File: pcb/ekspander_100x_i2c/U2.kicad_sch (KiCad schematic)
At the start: 13 parts, among them J5 DG127A-5.08-06P-14-00AH, J6 DG127A-5.08-06P-14-00AH, J7 DG127A-5.08-06P-14-00AH, U14 LTV-847, U15 ITS716G, U16 ITS716G, U17 LTV-847, U18 LTV-847, U2 MCP23017_SP

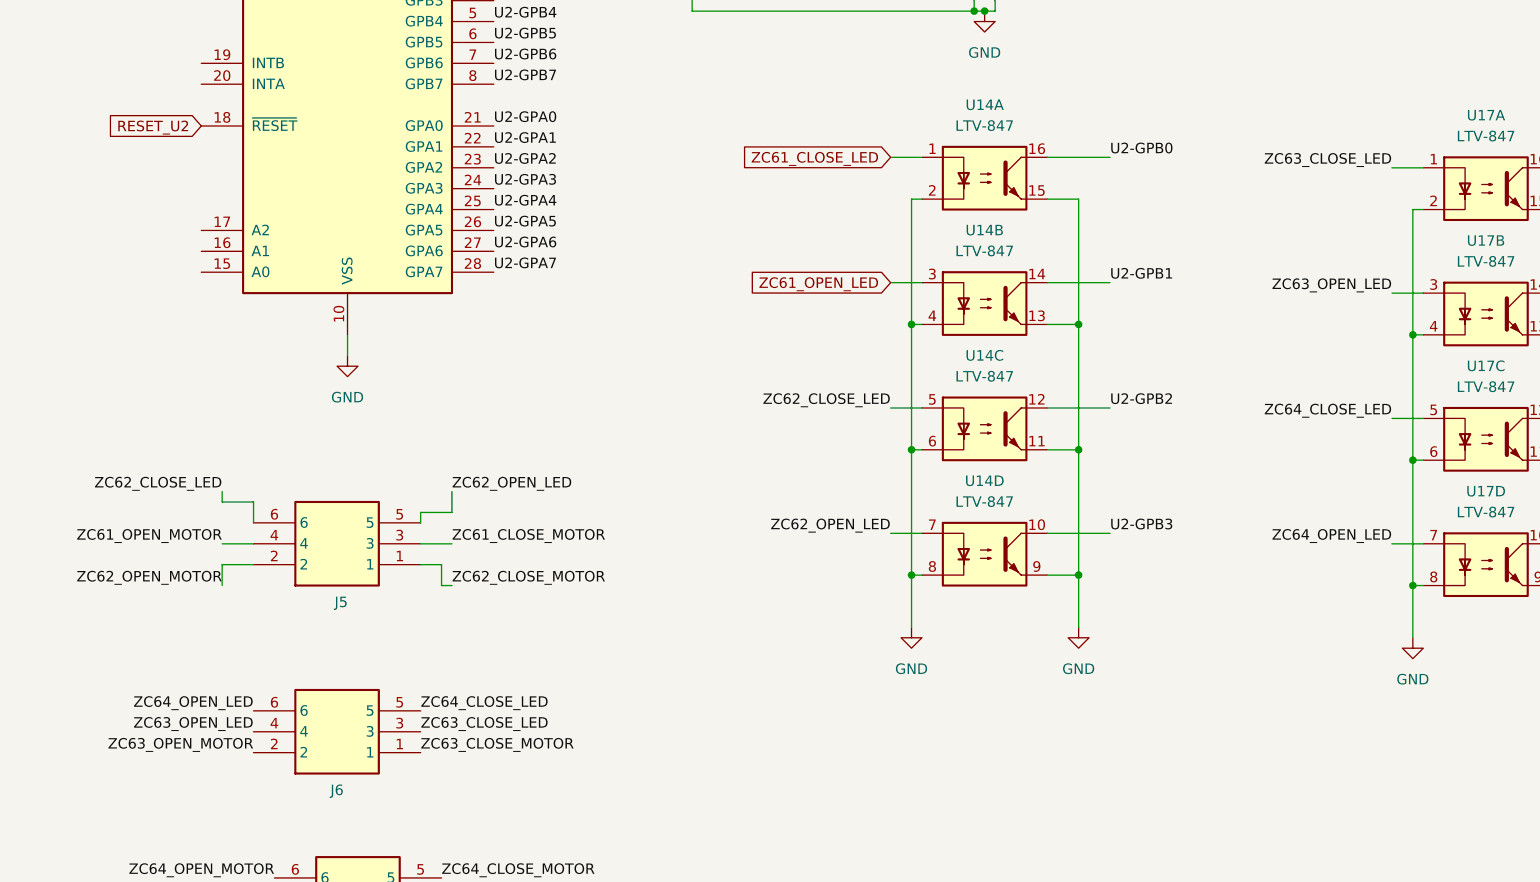
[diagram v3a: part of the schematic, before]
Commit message: Ekspander 100x - finish J
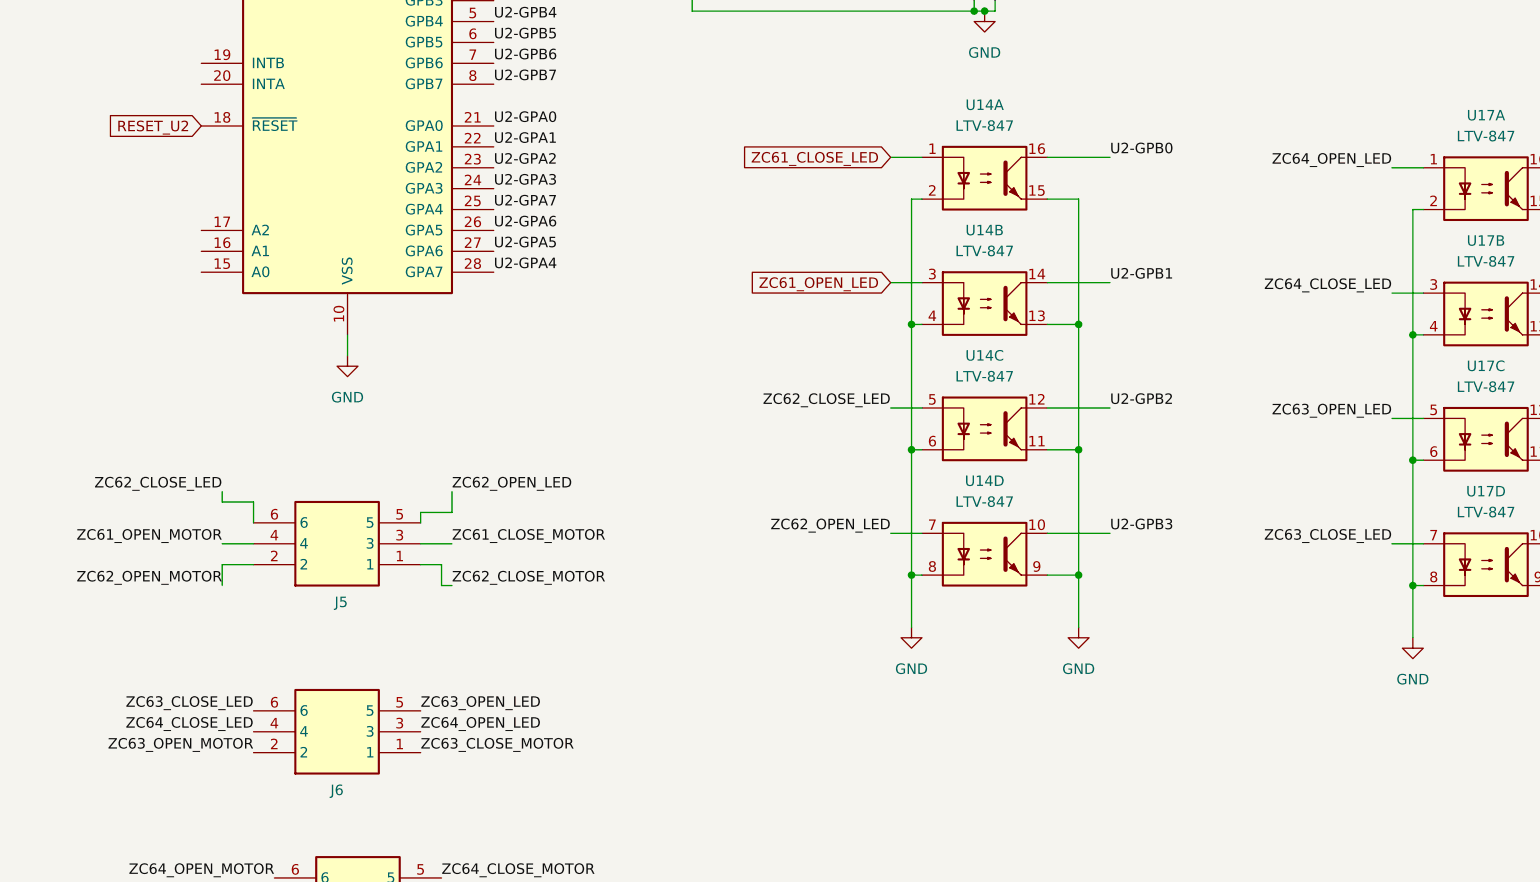
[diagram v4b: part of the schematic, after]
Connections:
- net U2-GPA4: now also U2.28 (GPA7); no longer U2.25 (GPA4)
- net U2-GPA5: now also U2.27 (GPA6); no longer U2.26 (GPA5)
- net U2-GPA6: now also U2.26 (GPA5); no longer U2.27 (GPA6)
- net U2-GPA7: now also U2.25 (GPA4); no longer U2.28 (GPA7)
- net ZC63_CLOSE_LED: now also J6.6, U17.7; no longer J6.3, U17.1
- net ZC63_OPEN_LED: now also J6.5, U17.5; no longer J6.4, U17.3
- net ZC64_CLOSE_LED: now also J6.4, U17.3; no longer J6.5, U17.5
- net ZC64_OPEN_LED: now also J6.3, U17.1; no longer J6.6, U17.7
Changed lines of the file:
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@@
 	)
 	(label "ZC64_OPEN_LED"
-		(at 179.07 119.38 180)
+		(at 179.07 73.66 180)
 		(effects
 			(font
@@
 	)
 	(label "ZC64_OPEN_LED"
-		(at 40.64 139.7 180)
-		(effects
-			(font
-				(size 1.27 1.27)
-			)
-			(justify right bottom)
+		(at 60.96 142.24 0)
+		(effects
+			(font
+				(size 1.27 1.27)
+			)
+			(justify left bottom)
 		)
 	)
@@
 	)
 	(label "ZC63_CLOSE_LED"
-		(at 60.96 142.24 0)
-		(effects
-			(font
-				(size 1.27 1.27)
-			)
-			(justify left bottom)
+		(at 40.64 139.7 180)
+		(effects
+			(font
+				(size 1.27 1.27)
+			)
+			(justify right bottom)
 		)
 	)
 	(label "U2-GPA6"
-		(at 69.85 83.82 0)
-		(effects
-			(font
-				(size 1.27 1.27)
-			)
-			(justify left bottom)
-		)
-		(property "Netclass" "GPIO"
-			(at 79.756 83.82 0)
+		(at 69.85 81.28 0)
+		(effects
+			(font
+				(size 1.27 1.27)
+			)
+			(justify left bottom)
+		)
+		(property "Netclass" "GPIO"
+			(at 79.756 81.28 0)
 			(effects
 				(font
@@
 	)
 	(label "ZC64_CLOSE_LED"
-		(at 60.96 139.7 0)
-		(effects
-			(font
-				(size 1.27 1.27)
-			)
-			(justify left bottom)
+		(at 40.64 142.24 180)
+		(effects
+			(font
+				(size 1.27 1.27)
+			)
+			(justify right bottom)
 		)
 	)
@@
 	)
 	(label "ZC63_OPEN_LED"
-		(at 40.64 142.24 180)
-		(effects
-			(font
-				(size 1.27 1.27)
-			)
-			(justify right bottom)
+		(at 60.96 139.7 0)
+		(effects
+			(font
+				(size 1.27 1.27)
+			)
+			(justify left bottom)
 		)
 	)
@@
 	)
 	(label "U2-GPA5"
-		(at 69.85 81.28 0)
-		(effects
-			(font
-				(size 1.27 1.27)
-			)
-			(justify left bottom)
-		)
-		(property "Netclass" "GPIO"
-			(at 79.756 81.28 0)
+		(at 69.85 83.82 0)
+		(effects
+			(font
+				(size 1.27 1.27)
+			)
+			(justify left bottom)
+		)
+		(property "Netclass" "GPIO"
+			(at 79.756 83.82 0)
 			(effects
 				(font
@@
 	)
 	(label "U2-GPA4"
-		(at 69.85 78.74 0)
-		(effects
-			(font
-				(size 1.27 1.27)
-			)
-			(justify left bottom)
-		)
-		(property "Netclass" "GPIO"
-			(at 79.756 78.74 0)
+		(at 69.85 86.36 0)
+		(effects
+			(font
+				(size 1.27 1.27)
+			)
+			(justify left bottom)
+		)
+		(property "Netclass" "GPIO"
+			(at 79.756 86.36 0)
 			(effects
 				(font
@@
 	)
 	(label "ZC63_CLOSE_LED"
-		(at 179.07 73.66 180)
+		(at 179.07 119.38 180)
 		(effects
 			(font
@@
 	)
 	(label "U2-GPA7"
-		(at 69.85 86.36 0)
-		(effects
-			(font
-				(size 1.27 1.27)
-			)
-			(justify left bottom)
-		)
-		(property "Netclass" "GPIO"
-			(at 79.756 86.36 0)
+		(at 69.85 78.74 0)
+		(effects
+			(font
+				(size 1.27 1.27)
+			)
+			(justify left bottom)
+		)
+		(property "Netclass" "GPIO"
+			(at 79.756 78.74 0)
 			(effects
 				(font
@@
 	)
 	(label "ZC64_CLOSE_LED"
-		(at 179.07 104.14 180)
+		(at 179.07 88.9 180)
 		(effects
 			(font
@@
 	)
 	(label "ZC63_OPEN_LED"
-		(at 179.07 88.9 180)
-		(effects
-			(font
+		(at 179.07 104.14 180)
+		(effects
+			(font

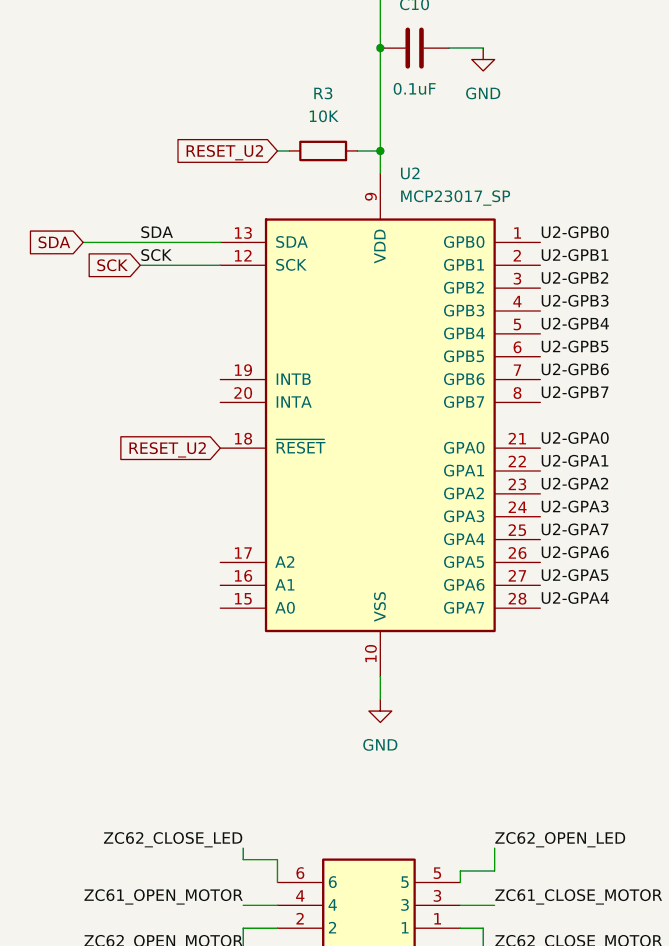
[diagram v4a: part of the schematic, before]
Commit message: Ekspander 100x - adresacja I2C - MCP23017
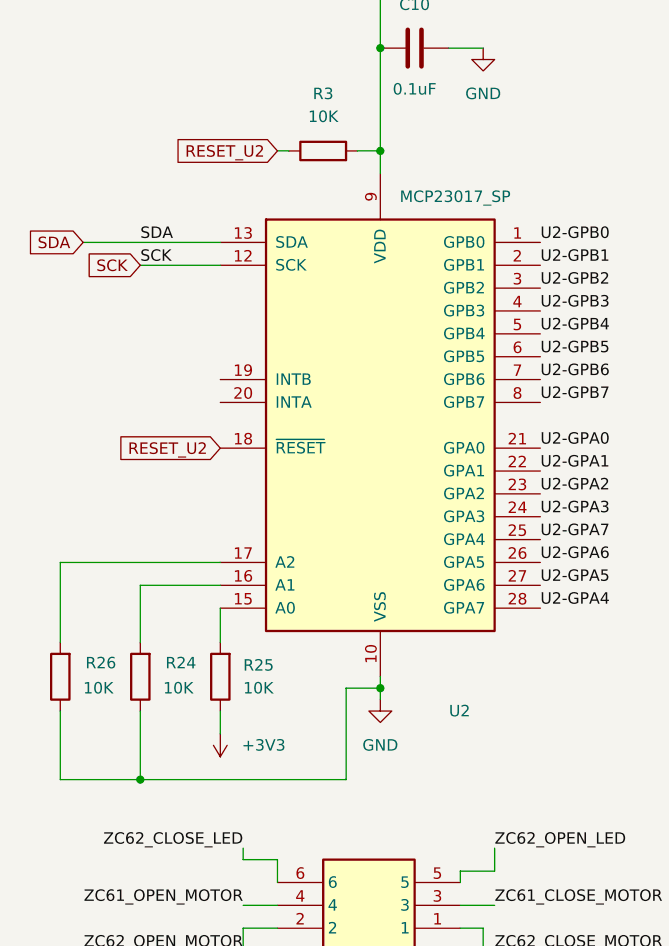
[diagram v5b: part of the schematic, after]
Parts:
- added R24, R25, R26: 10K, PCM_Resistor_SMD_AKL:R_0805_2012Metric_Pad1.20x1.40mm_HandSolder, symbol Device:R
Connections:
- net +3V3: now also R25.1
- net GND: now also R24.1, R26.1
- net at U2.15 (A0): now also R25.2
- net at U2.16 (A1): now also R24.2
- net at U2.17 (A2): now also R26.2

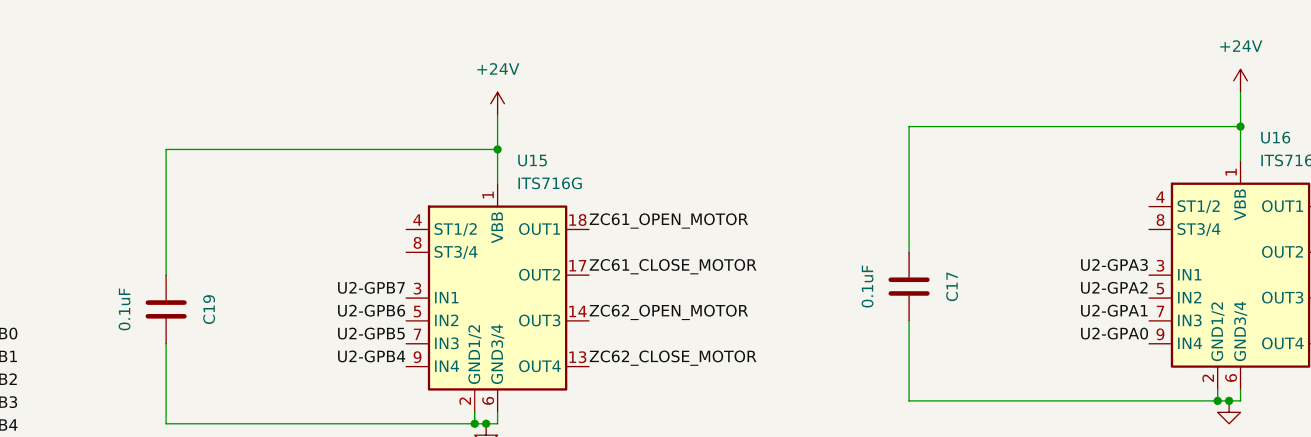
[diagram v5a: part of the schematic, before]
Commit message: Ekspander 100x - diagnostic LEDs
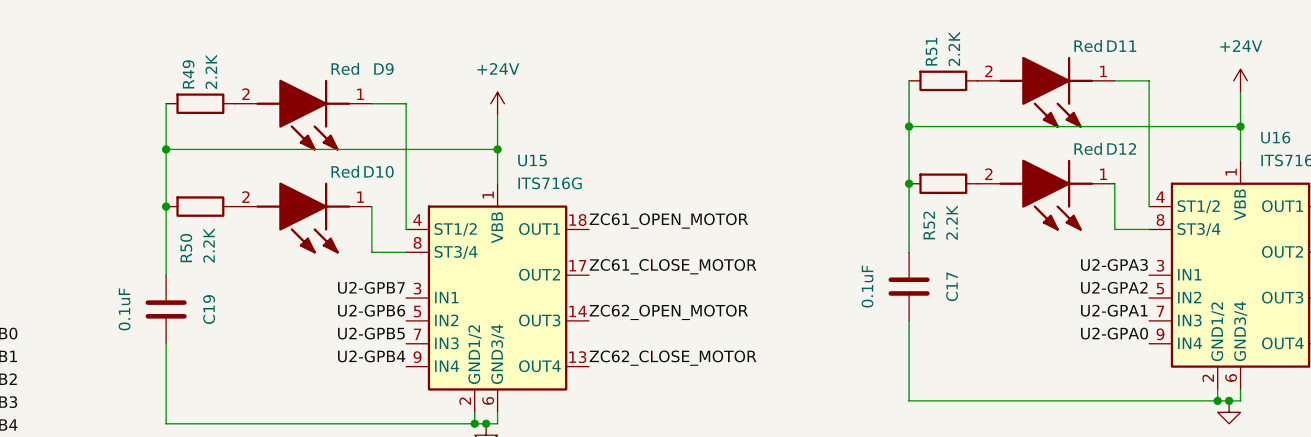
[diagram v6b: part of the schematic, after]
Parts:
- added D10, D11, D12, D9: Red, 1_tme:LEDC2012X120N, symbol LTST-C170KRKT:LTST-C170KRKT
- added R49, R50, R51, R52: 2.2K, PCM_Resistor_SMD_AKL:R_0805_2012Metric_Pad1.20x1.40mm_HandSolder, symbol Device:R
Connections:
- net +24V: now also R49.2, R50.2, R51.2, R52.2
- net at U15.4 (ST1/2): now also D9.1 (K)
- net at U15.8 (ST3/4): now also D10.1 (K)
- net at U16.4 (ST1/2): now also D11.1 (K)
- net at U16.8 (ST3/4): now also D12.1 (K)
- new net: D12.2 (A), R52.1
- new net: D11.2 (A), R51.1
- new net: D9.2 (A), R49.1
- new net: D10.2 (A), R50.1
